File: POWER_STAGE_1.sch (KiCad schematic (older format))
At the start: 13 parts, among them IC601 BTN8962TA

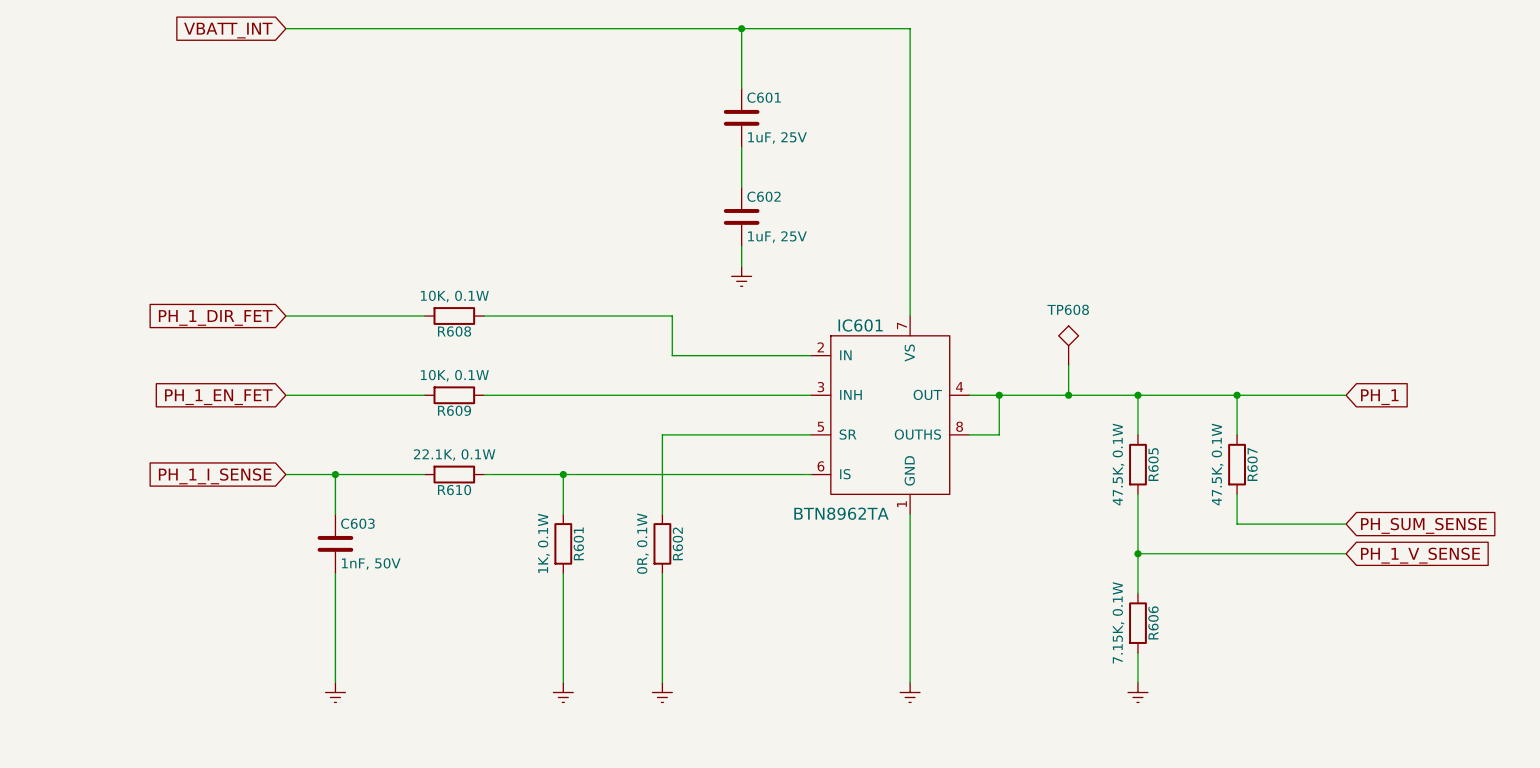
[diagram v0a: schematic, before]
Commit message: - Finished adaptation to JMS board footprint. - Added testpoints. - Changed header connector to 0.1" pitch, and tall.
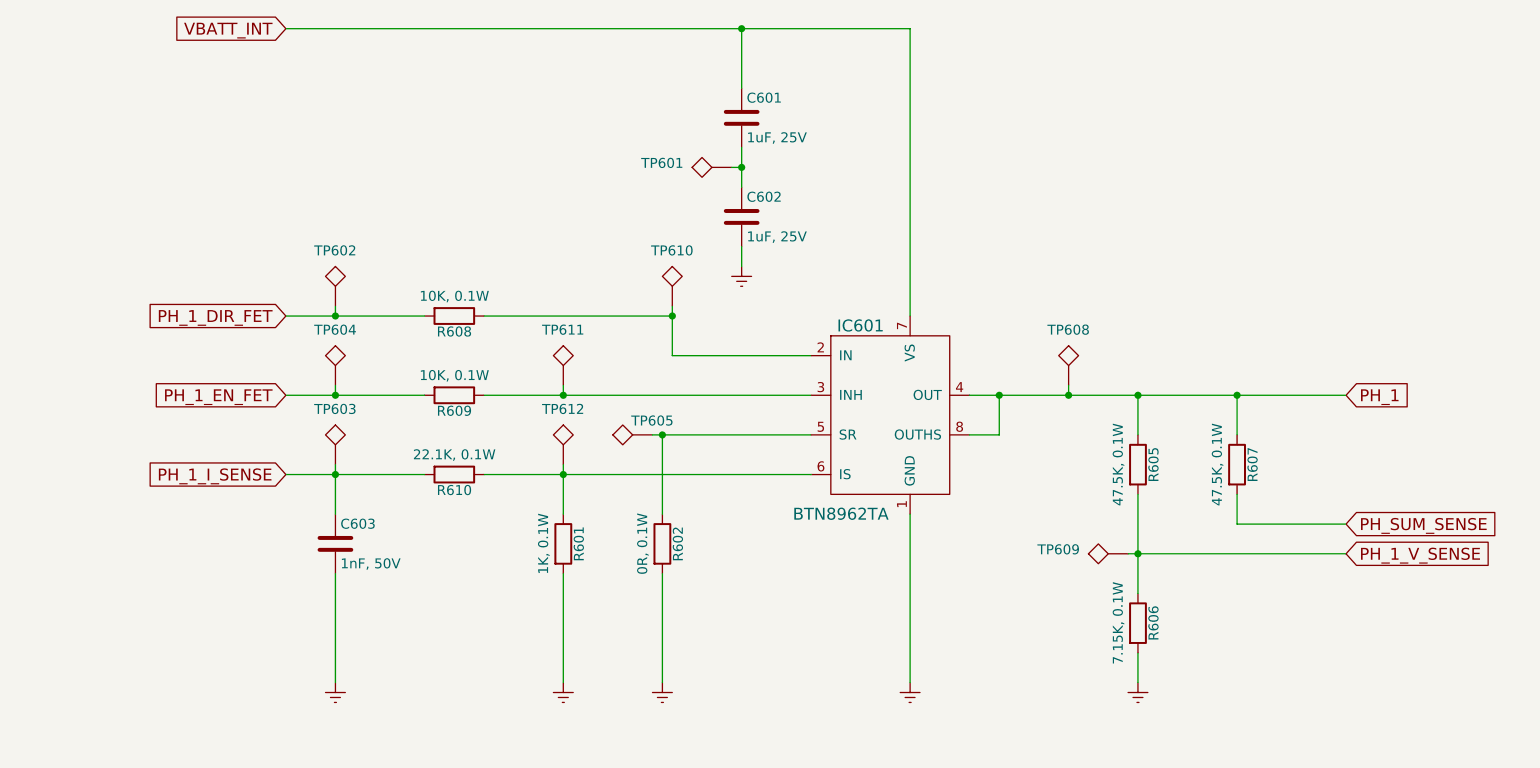
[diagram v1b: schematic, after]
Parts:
- added TP601, TP602, TP603, TP604, TP605, TP609, TP610, TP611, TP612: TEST, hp-bldc-pcb:TEST_POINT_40mil, symbol TEST
- TP608: footprint Measurement_Points:Measurement_Point_Round-SMD-Pad_Big -> hp-bldc-pcb:TEST_POINT_40mil
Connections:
- net PH_1_DIR_FET: now also TP602.1
- net PH_1_EN_FET: now also TP604.1
- net PH_1_I_SENSE: now also TP603.1
- net PH_1_V_SENSE: now also TP609.1
- net at IC601.2 (IN), R608.1: now also TP610.1
- net at IC601.3 (INH), R609.1: now also TP611.1
- net at IC601.5 (SR), R602.1: now also TP605.1
- net at IC601.6 (IS), R601.1, R610.1: now also TP612.1
- net at C601.2, C602.1: now also TP601.1
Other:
- moved on the sheet: TP608
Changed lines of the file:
@@
 	4100 3200 5050 3200
 Wire Wire Line
-	5050 3200 5050 3400
+	5050 3150 5050 3400
 Wire Wire Line
 	5050 3400 5750 3400
@@
 $EndComp
 Wire Wire Line
-	3350 4200 3350 4000
+	3350 3950 3350 4200
 Connection ~ 3350 4000
 $Comp
-L Earth #PWR037
+L Earth #PWR038
 U 1 1 5A79F9D5
 P 3350 5050
-F 0 "#PWR037" H 3350 4800 50  0001 C CNN
+F 0 "#PWR038" H 3350 4800 50  0001 C CNN
 F 1 "Earth" H 3350 4900 50  0001 C CNN
 F 2 "" H 3350 5050 50  0001 C CNN
@@
 $EndComp
 Wire Wire Line
-	4500 4200 4500 4000
+	4500 3950 4500 4200
 Connection ~ 4500 4000
 Wire Wire Line
 	5000 4200 5000 3800
 Wire Wire Line
-	5000 3800 5750 3800
-$Comp
-L Earth #PWR038
+	4950 3800 5750 3800
+$Comp
+L Earth #PWR039
 U 1 1 5A79FE9C
 P 4500 5050
-F 0 "#PWR038" H 4500 4800 50  0001 C CNN
+F 0 "#PWR039" H 4500 4800 50  0001 C CNN
 F 1 "Earth" H 4500 4900 50  0001 C CNN
 F 2 "" H 4500 5050 50  0001 C CNN
@@
 	4500 4500 4500 5050
 $Comp
-L Earth #PWR039
+L Earth #PWR040
 U 1 1 5A79FED4
 P 5000 5050
-F 0 "#PWR039" H 5000 4800 50  0001 C CNN
+F 0 "#PWR040" H 5000 4800 50  0001 C CNN
 F 1 "Earth" H 5000 4900 50  0001 C CNN
 F 2 "" H 5000 5050 50  0001 C CNN
@@
 	5000 4500 5000 5050
 $Comp
-L Earth #PWR040
+L Earth #PWR041
 U 1 1 5A79FF15
 P 6250 5050
-F 0 "#PWR040" H 6250 4800 50  0001 C CNN
+F 0 "#PWR041" H 6250 4800 50  0001 C CNN
 F 1 "Earth" H 6250 4900 50  0001 C CNN
 F 2 "" H 6250 5050 50  0001 C CNN
@@
 $EndComp
 $Comp
-L Earth #PWR041
+L Earth #PWR042
 U 1 1 5A7A0166
 P 5400 2950
-F 0 "#PWR041" H 5400 2700 50  0001 C CNN
+F 0 "#PWR042" H 5400 2700 50  0001 C CNN
 F 1 "Earth" H 5400 2800 50  0001 C CNN
 F 2 "" H 5400 2950 50  0001 C CNN
@@
 PH_1_V_SENSE
 Wire Wire Line
-	8450 4400 7400 4400
+	7350 4400 8450 4400
 Connection ~ 7400 4400
 $Comp
-L Earth #PWR042
+L Earth #PWR043
 U 1 1 5A7A08DC
 P 7400 5050
-F 0 "#PWR042" H 7400 4800 50  0001 C CNN
+F 0 "#PWR043" H 7400 4800 50  0001 C CNN
 F 1 "Earth" H 7400 4900 50  0001 C CNN
 F 2 "" H 7400 5050 50  0001 C CNN
@@
 L TEST TP608
 U 1 1 5A7A0ADB
-P 7050 3450
-F 0 "TP608" H 7050 3700 50  0000 C BNN
-F 1 "TEST" H 7050 3700 50  0001 C CNN
-F 2 "Measurement_Points:Measurement_Point_Round-SMD-Pad_Big" H 7050 3450 50  0001 C CNN
-F 3 "" H 7050 3450 50  0001 C CNN
-	1    7050 3450
-	1    0    0    -1
-$EndComp
-Wire Wire Line
-	7050 3450 7050 3600
+P 7050 3550
+F 0 "TP608" H 7050 3800 50  0000 C BNN
+F 1 "TEST" H 7050 3800 50  0001 C CNN
+F 2 "hp-bldc-pcb:TEST_POINT_40mil" H 7050 3550 50  0001 C CNN
+F 3 "" H 7050 3550 50  0001 C CNN
+	1    7050 3550
+	1    0    0    -1
+$EndComp
+Wire Wire Line
+	7050 3550 7050 3600
 Connection ~ 7050 3600
+$Comp
+L TEST TP602
+U 1 1 5AB3AB29
+P 3350 3150
+F 0 "TP602" H 3350 3400 50  0000 C BNN
+F 1 "TEST" H 3350 3400 50  0001 C CNN
+F 2 "hp-bldc-pcb:TEST_POINT_40mil" H 3350 3150 50  0001 C CNN
+F 3 "" H 3350 3150 50  0001 C CNN
+	1    3350 3150
+	1    0    0    -1
+$EndComp
+Wire Wire Line
+	3350 3150 3350 3200
+Connection ~ 3350 3200
+$Comp
+L TEST TP604
+U 1 1 5AB3ABCD
+P 3350 3550
+F 0 "TP604" H 3350 3800 50  0000 C BNN
+F 1 "TEST" H 3350 3800 50  0001 C CNN
+F 2 "hp-bldc-pcb:TEST_POINT_40mil" H 3350 3550 50  0001 C CNN
+F 3 "" H 3350 3550 50  0001 C CNN
+	1    3350 3550
+	1    0    0    -1
+$EndComp
+Wire Wire Line
+	3350 3550 3350 3600
+Connection ~ 3350 3600
+$Comp
+L TEST TP603
+U 1 1 5AB3AC52
+P 3350 3950
+F 0 "TP603" H 3350 4200 50  0000 C BNN
+F 1 "TEST" H 3350 4200 50  0001 C CNN
+F 2 "hp-bldc-pcb:TEST_POINT_40mil" H 3350 3950 50  0001 C CNN
+F 3 "" H 3350 3950 50  0001 C CNN
+	1    3350 3950
+	1    0    0    -1
+$EndComp
+$Comp
+L TEST TP611
+U 1 1 5AB3AD4F
+P 4500 3550
+F 0 "TP611" H 4500 3800 50  0000 C BNN
+F 1 "TEST" H 4500 3800 50  0001 C CNN
+F 2 "hp-bldc-pcb:TEST_POINT_40mil" H 4500 3550 50  0001 C CNN
+F 3 "" H 4500 3550 50  0001 C CNN
+	1    4500 3550
+	1    0    0    -1
+$EndComp
+Wire Wire Line
+	4500 3550 4500 3600
+Connection ~ 4500 3600
+$Comp
+L TEST TP612
+U 1 1 5AB3AE02
+P 4500 3950
+F 0 "TP612" H 4500 4200 50  0000 C BNN
+F 1 "TEST" H 4500 4200 50  0001 C CNN
+F 2 "hp-bldc-pcb:TEST_POINT_40mil" H 4500 3950 50  0001 C CNN
+F 3 "" H 4500 3950 50  0001 C CNN
+	1    4500 3950
+	1    0    0    -1
+$EndComp
+$Comp
+L TEST TP605
+U 1 1 5AB3AEEC
+P 4950 3800
+F 0 "TP605" V 5050 3800 50  0000 C BNN
+F 1 "TEST" H 4950 4050 50  0001 C CNN
+F 2 "hp-bldc-pcb:TEST_POINT_40mil" H 4950 3800 50  0001 C CNN
+F 3 "" H 4950 3800 50  0001 C CNN
+	1    4950 3800
+	0    -1   -1   0
+$EndComp
+Connection ~ 5000 3800
+$Comp
+L TEST TP610
+U 1 1 5AB3B062
+P 5050 3150
+F 0 "TP610" H 5050 3400 50  0000 C BNN
+F 1 "TEST" H 5050 3400 50  0001 C CNN
+F 2 "hp-bldc-pcb:TEST_POINT_40mil" H 5050 3150 50  0001 C CNN
+F 3 "" H 5050 3150 50  0001 C CNN
+	1    5050 3150
+	1    0    0    -1
+$EndComp
+Connection ~ 5050 3200
+$Comp
+L TEST TP601
+U 1 1 5AB3B153
+P 5350 2450
+F 0 "TP601" V 5400 2800 50  0000 C BNN
+F 1 "TEST" H 5350 2700 50  0001 C CNN
+F 2 "hp-bldc-pcb:TEST_POINT_40mil" H 5350 2450 50  0001 C CNN
+F 3 "" H 5350 2450 50  0001 C CNN
+	1    5350 2450
+	0    -1   -1   0
+$EndComp
+Wire Wire Line
+	5350 2450 5400 2450
+Connection ~ 5400 2450
+$Comp
+L TEST TP609
+U 1 1 5AB3B36C
+P 7350 4400
+F 0 "TP609" V 7400 4750 50  0000 C BNN
+F 1 "TEST" H 7350 4650 50  0001 C CNN
+F 2 "hp-bldc-pcb:TEST_POINT_40mil" H 7350 4400 50  0001 C CNN
+F 3 "" H 7350 4400 50  0001 C CNN
+	1    7350 4400
+	0    -1   -1   0
+$EndComp
 $EndSCHEMATC

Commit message: - Minor changes to silkscreen. - Minor changes to BOM. - Additions to Readme file. - Page layout changed in schematic.
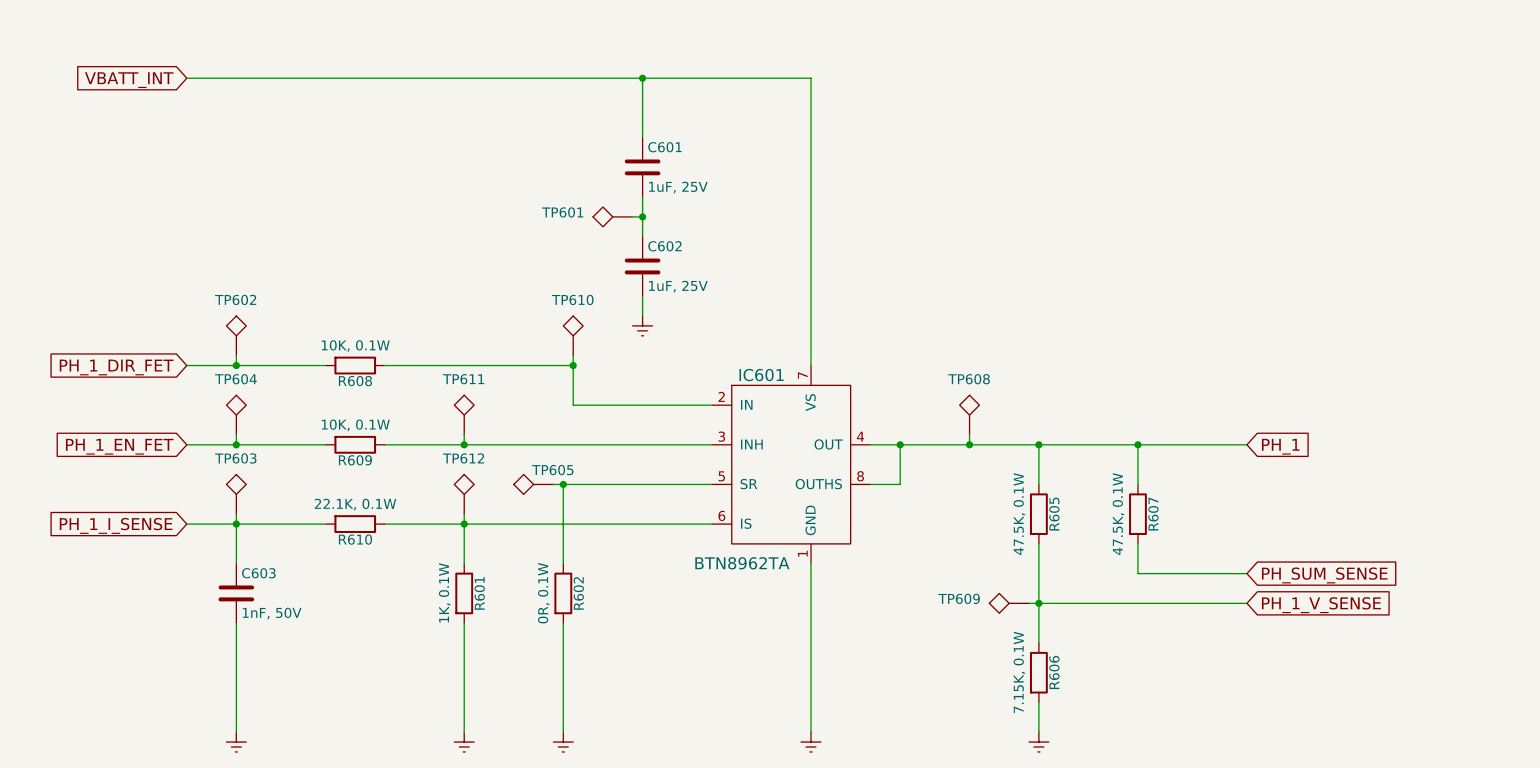
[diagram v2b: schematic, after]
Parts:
- IC601: footprint TO_SOT_Packages_SMD:TO-263-7_TabPin8 -> hp-bldc-pcb:TO-263-7_TabPin8
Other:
- moved on the sheet: C601, C602, C603, IC601, R601, R602, R605, R606, R607, R608, R609, R610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
